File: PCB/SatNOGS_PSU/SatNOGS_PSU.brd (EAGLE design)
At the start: 67 x 45.7 mm, 5 parts, among them X4 USB_3PSHIELD-85-32003-00X-1

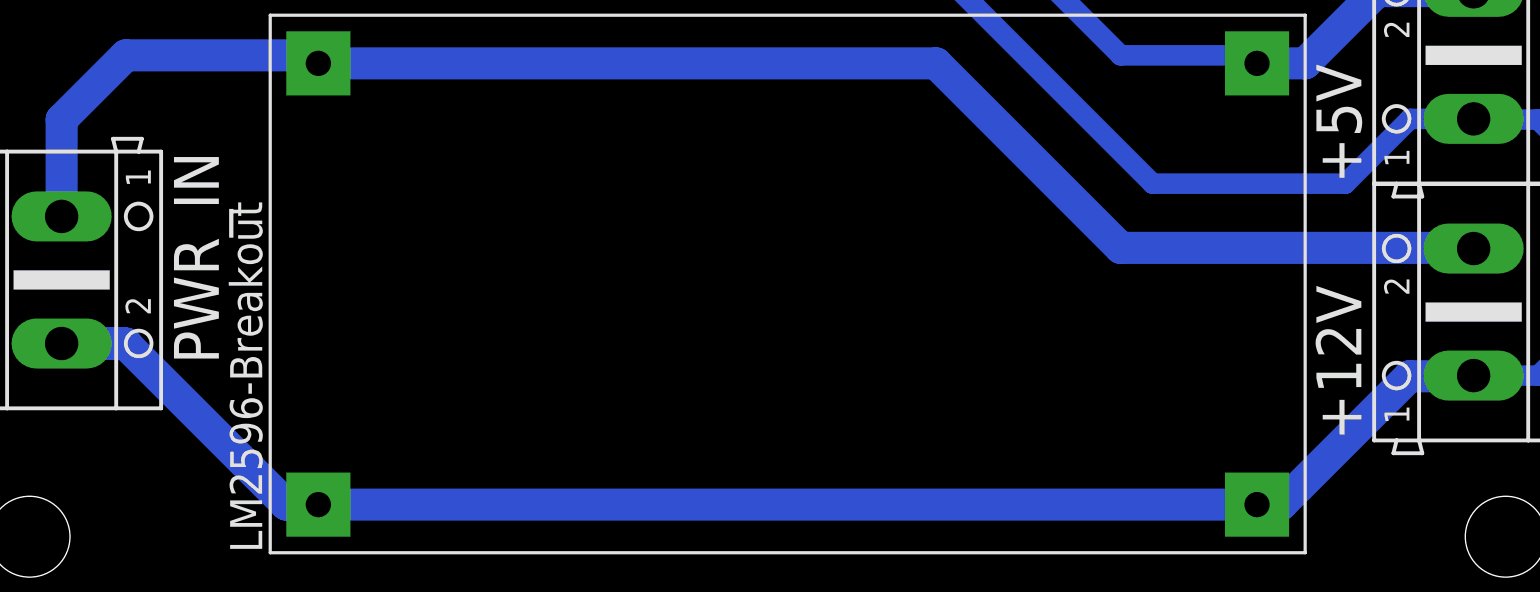
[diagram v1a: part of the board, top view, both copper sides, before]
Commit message: Change names in Top Silkscreen.
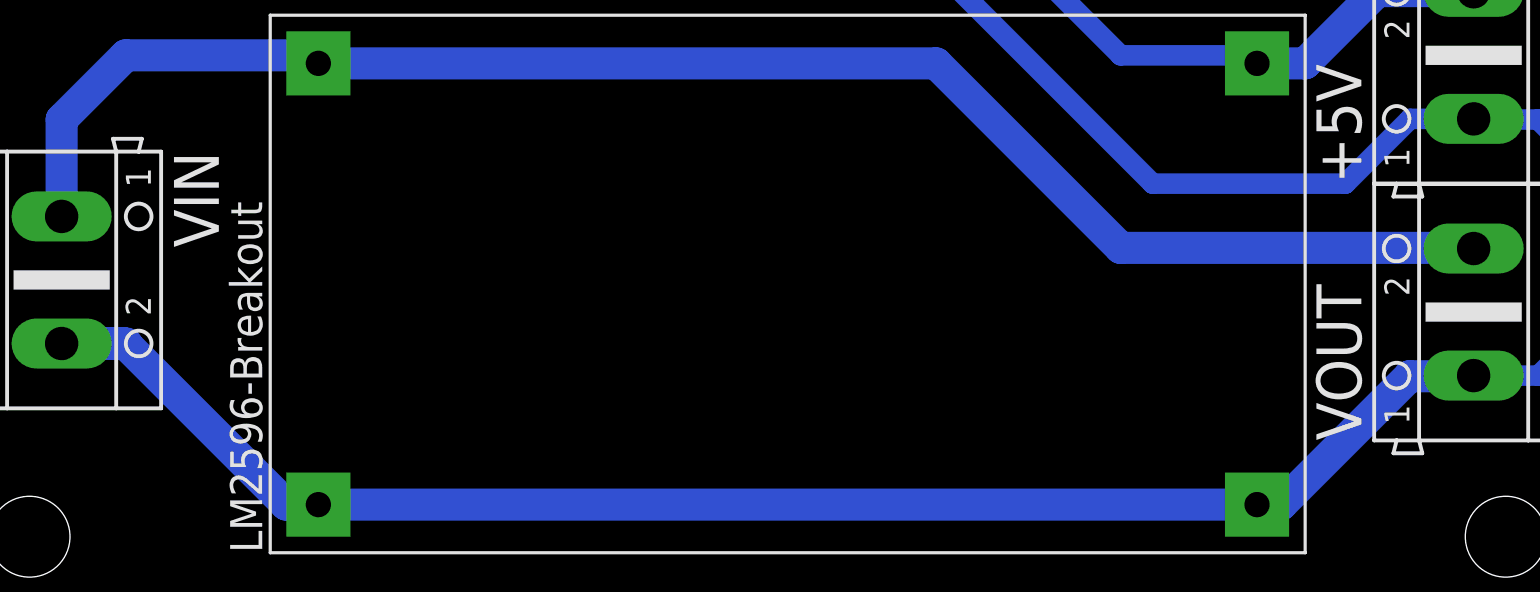
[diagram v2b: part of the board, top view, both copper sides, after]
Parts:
- renumbered +12V to VOUT, PWR_IN to VIN, U$1 to LM2596
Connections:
- net +12V renamed VIN
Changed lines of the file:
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@@
 <?xml version="1.0" encoding="utf-8"?>
 <!DOCTYPE eagle SYSTEM "eagle.dtd">
-<eagle version="7.1.0">
+<eagle version="7.2.0">
 <drawing>
 <settings>
@@
 <layer number="25" name="tNames" color="7" fill="1" visible="yes" active="yes"/>
 <layer number="26" name="bNames" color="7" fill="1" visible="yes" active="yes"/>
-<layer number="27" name="tValues" color="7" fill="1" visible="yes" active="yes"/>
-<layer number="28" name="bValues" color="7" fill="1" visible="yes" active="yes"/>
+<layer number="27" name="tValues" color="7" fill="1" visible="no" active="yes"/>
+<layer number="28" name="bValues" color="7" fill="1" visible="no" active="yes"/>
 <layer number="29" name="tStop" color="7" fill="3" visible="yes" active="yes"/>
 <layer number="30" name="bStop" color="7" fill="6" visible="yes" active="yes"/>
@@
 </autorouter>
 <elements>
-<element name="U$1" library="LM2596-Breakout" package="LM2596-BREAKOUT" value="LM2596-BREAKOUTLM2596-BREAKOUT" x="33.02" y="12.7" rot="R90"/>
-<element name="PWR_IN" library="con-ptr500" package="AK500/2" value="1" x="5.08" y="12.7" rot="R270">
+<element name="LM2596" library="LM2596-Breakout" package="LM2596-BREAKOUT" value="LM2596-BREAKOUTLM2596-BREAKOUT" x="33.02" y="12.7" rot="R90"/>
+<element name="VIN" library="con-ptr500" package="AK500/2" value="1" x="5.08" y="12.7" rot="R270">
 <attribute name="OC_NEWARK" value="unknown" x="-41.91" y="-24.13" size="1.778" layer="27" rot="R270" display="off"/>
 <attribute name="MPN" value="" x="-41.91" y="-24.13" size="1.778" layer="27" rot="R270" display="off"/>
@@
 <attribute name="OC_FARNELL" value="unknown" x="-41.91" y="-24.13" size="1.778" layer="27" rot="R270" display="off"/>
 </element>
-<element name="+12V" library="con-ptr500" package="AK500/2" value="2" x="60.96" y="11.43" rot="R90">
+<element name="VOUT" library="con-ptr500" package="AK500/2" value="2" x="60.96" y="11.43" rot="R90">
 <attribute name="OC_NEWARK" value="unknown" x="107.95" y="59.69" size="1.778" layer="27" rot="R90" display="off"/>
 <attribute name="MPN" value="" x="107.95" y="59.69" size="1.778" layer="27" rot="R90" display="off"/>
@@
 </elements>
 <signals>
-<signal name="+12V">
-<contactref element="U$1" pad="4"/>
-<contactref element="+12V" pad="2"/>
-<contactref element="PWR_IN" pad="1"/>
+<signal name="VIN">
+<contactref element="LM2596" pad="4"/>
+<contactref element="VOUT" pad="2"/>
+<contactref element="VIN" pad="1"/>
 <wire x1="46.99" y1="13.97" x2="62.23" y2="13.97" width="1.27" layer="16"/>
 <wire x1="62.23" y1="13.97" x2="60.96" y2="13.9446" width="1.27" layer="16"/>
@@
 </signal>
 <signal name="+5V">
-<contactref element="U$1" pad="3"/>
+<contactref element="LM2596" pad="3"/>
 <contactref element="+5V" pad="2"/>
 <wire x1="52.3875" y1="21.2725" x2="54.2925" y2="21.2725" width="1.27" layer="16"/>
@@
 </signal>
 <signal name="GND">
-<contactref element="PWR_IN" pad="2"/>
-<contactref element="U$1" pad="1"/>
-<contactref element="U$1" pad="2"/>
-<contactref element="+12V" pad="1"/>
+<contactref element="VIN" pad="2"/>
+<contactref element="LM2596" pad="1"/>
+<contactref element="LM2596" pad="2"/>
+<contactref element="VOUT" pad="1"/>
 <contactref element="+5V" pad="1"/>
 <wire x1="5.08" y1="10.1854" x2="7.5946" y2="10.1854" width="1.27" layer="16"/>
